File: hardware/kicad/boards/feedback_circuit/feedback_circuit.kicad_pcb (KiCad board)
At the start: 2 copper layers, 118 x 50 mm, 10 parts, among them J1 ind + forsyning, J2 FB ud, U1 IL300, U3 MCP601, U4 MCP601

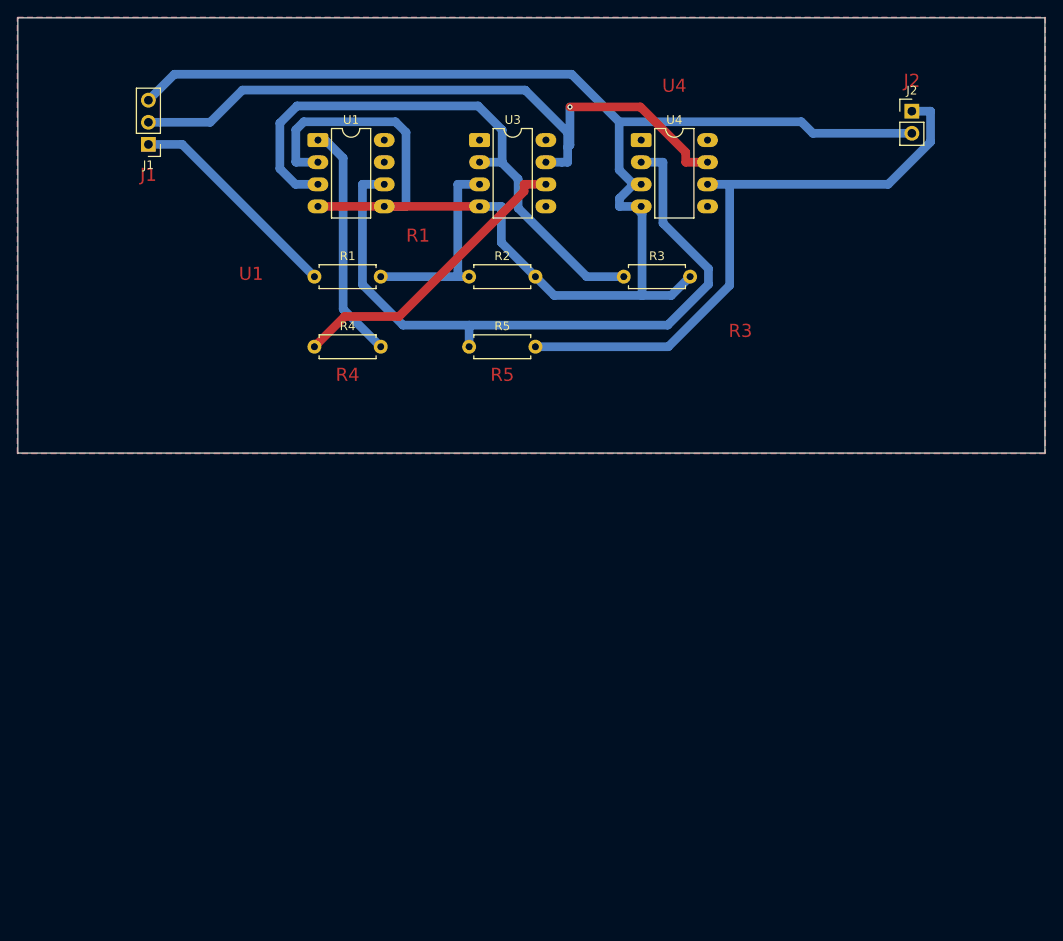
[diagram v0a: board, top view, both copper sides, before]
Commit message: Move all boards to the 104x104 jig format with compact placement
The laser positioning jig takes an exactly 109x109 mm copper blank, so every
board now has identical 104x104 edge cuts (2.5 mm rim). pcb_build.py:
- fixed JIG_W/JIG_H outline, hard failure if content overflows the square
- compact packing: 5 mm bbox gaps (was 8), squarish component cluster below
  the connector zone instead of full-width rows
- mppt/current_sense PLACE layouts re-arranged for the square and tightened

All 7 boards rerouted: 0 unconnected, 0 real DRC errors, and no vias needed
anywhere (the square format routes better than the old elongated boards).
Production DXF/gerbers re-exported; README run-plan updated for the jig
(cut blanks to exactly 109x109, all boards share the same size now).
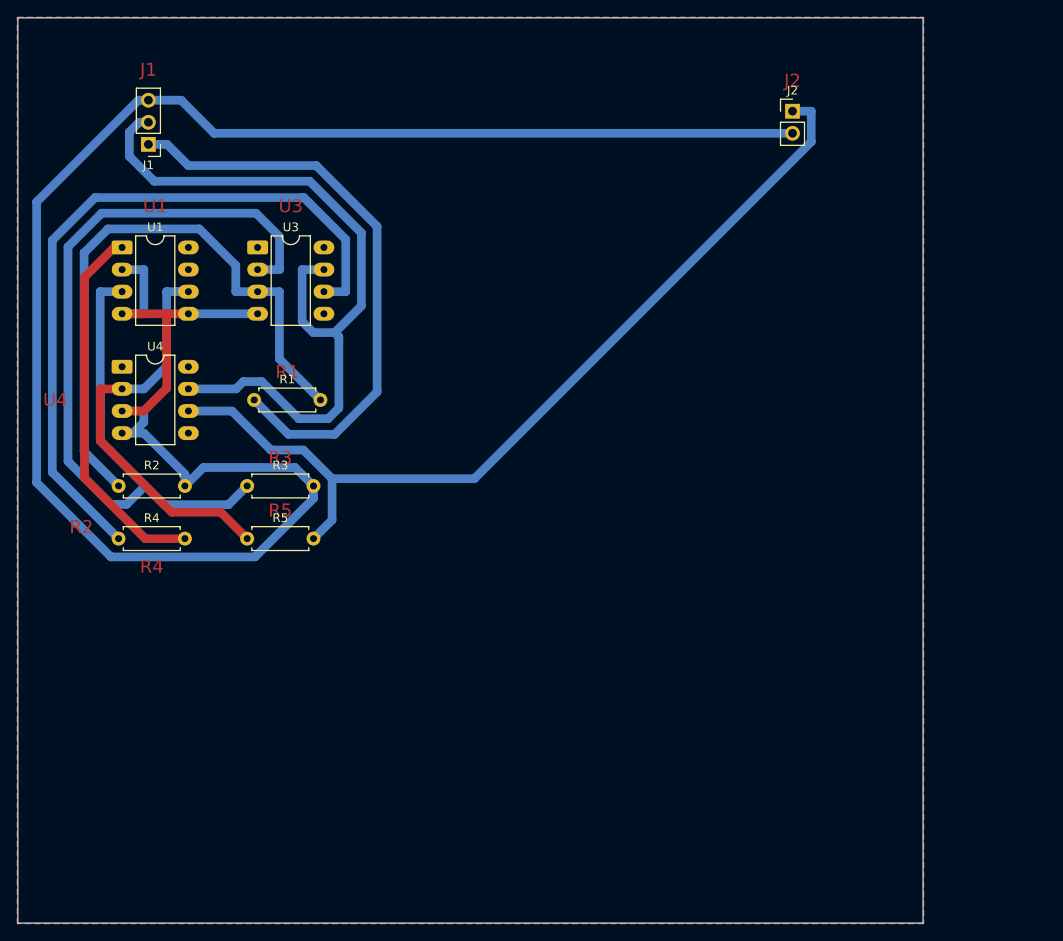
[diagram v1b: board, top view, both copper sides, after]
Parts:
- moved U4 65.1 mm to (32.0, 60.1)
- moved R3 49.5 mm to (46.3, 73.8)
- moved R2 46.9 mm to (31.6, 73.8)
- moved R5 33.7 mm to (46.3, 79.8)
- moved R4 31.5 mm to (31.6, 79.8)
- moved U3 28.3 mm to (47.5, 46.4)
- moved U1 25.7 mm to (32.0, 46.4)
- moved R1 15.8 mm to (47.1, 63.9)
- moved J2 13.7 mm to (109.0, 30.7)
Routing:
- net /U3_OUT: track 34.8 -> 83.7 mm
- net /IN_P: track 23.3 -> 71.1 mm
- net /SERVO: track 65.6 -> 110.2 mm
- net INPUT: track 25.4 -> 67.0 mm
- net GND: track 197.9 -> 238.1 mm
- net FB_OUT: track 70.2 -> 104.2 mm
- net /OUT_PD: track 78.8 -> 47.2 mm
- net /LED: track 27.2 -> 43.2 mm
- net +5V: track 81.5 -> 90.0 mm, vias 1 -> 0
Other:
- board size 118 x 50 mm -> 104 x 104 mm
- board text added: "R2"
- board text added: "U3"

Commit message: Condense and center all boards in the jig outline; reroute drive_circuit
Placement (pcb_build.py): connector columns now hug the component block
instead of sitting at the board edges, and the whole cluster is translated to
the center of the 104x104 outline - nothing sits next to the edge cuts
anymore. Fail-hard check if a cluster outgrows the jig.

drive_circuit keeps the hand-made GUI placement but is rerouted with the
two-stage flow: 43 top tracks + 1 via from the GUI autoroute down to 20
pin-to-pin bridges, no via. New tools/strip_routing.py removes existing
routing textually (sexpdata) - in-process pcbnew Remove() access-violates.

All 7 boards: 0 unconnected, 0 real DRC errors, no vias anywhere; buck is
now fully single-sided (0 top tracks). Production files re-exported.
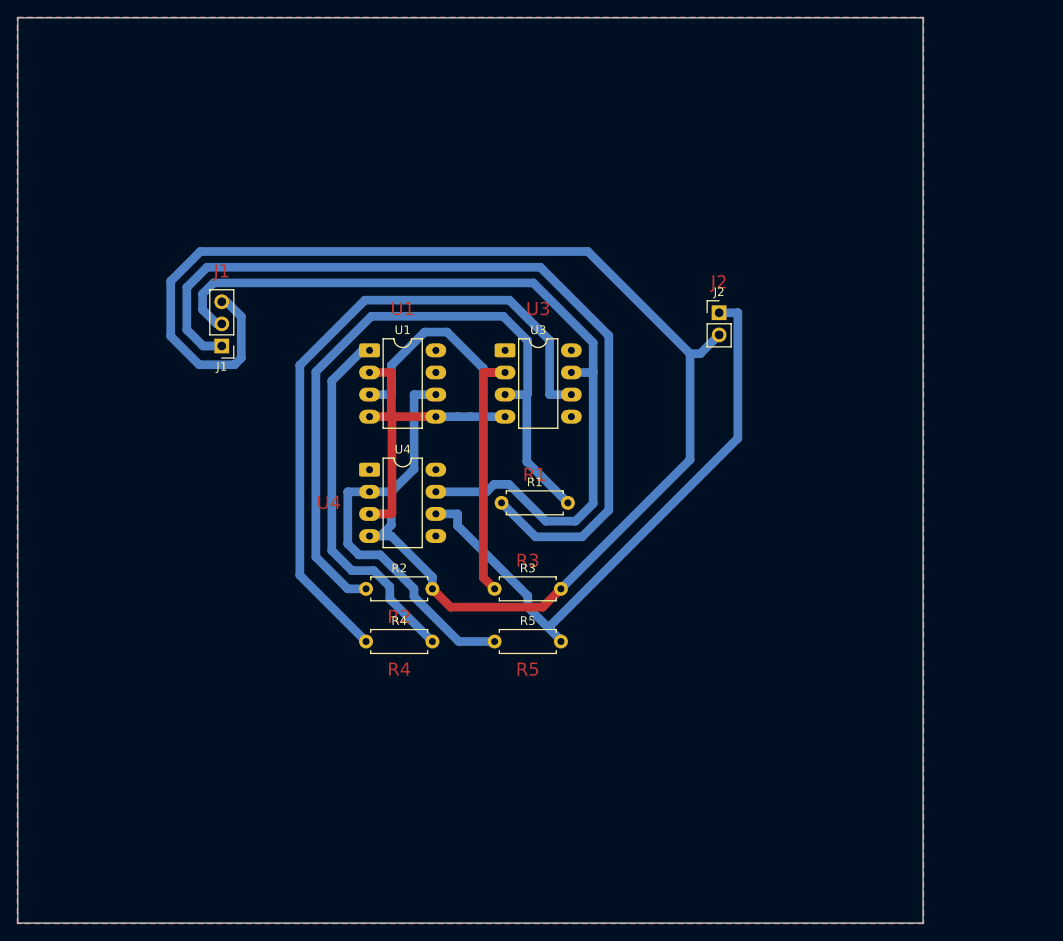
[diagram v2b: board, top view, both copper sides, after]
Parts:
- moved R2 30.8 mm to (60.0, 85.6)
- moved R4 30.8 mm to (60.0, 91.7)
- moved R3 30.8 mm to (74.8, 85.6)
- moved R5 30.8 mm to (74.8, 91.7)
- moved R1 30.8 mm to (75.6, 75.7)
- moved U1 30.8 mm to (60.4, 58.2)
- moved U4 30.8 mm to (60.4, 71.9)
- moved U3 30.8 mm to (76.0, 58.2)
- moved J2 24.6 mm to (100.6, 53.9)
- moved J1 24.6 mm to (43.4, 57.7)
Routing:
- net /SERVO: track 110.2 -> 50.6 mm
- net GND: track 238.1 -> 196.6 mm
- net FB_OUT: track 104.2 -> 69.4 mm
- net INPUT: track 67.0 -> 97.6 mm
- net /IN_P: track 71.1 -> 79.8 mm
- net /U3_OUT: track 83.7 -> 77.3 mm
- net +5V: track 90.0 -> 94.9 mm
- net /LED: track 43.2 -> 42.0 mm
- net /OUT_PD: track 47.2 -> 47.8 mm
